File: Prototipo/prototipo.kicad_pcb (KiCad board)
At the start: 2 copper layers, 271.5 x 102.5 mm, 139 parts, among them J1 Conn_01x02_Socket, J4 Conn_01x12_Pin, Q1 MMBT2222A, Q10 MMBT2222A, Q11 MMBT2907A, Q12 MMBT2222A, Q13 MMBT2222A, Q14 MMBT2907A, Q15 MMBT2222A, Q16 MMBT2222A, Q17 MMBT2907A, Q18 MMBT2222A, Q2 MMBT2222A, Q20 FDMS6681Z, Q21 FDMS6681Z, Q3 MMBT2907A, Q4 MMBT2222A, Q5 MMBT2907A, Q6 MMBT2222A, Q7 MMBT2907A, Q8 MMBT2222A, Q9 MMBT2222A

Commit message: Agrega los fusibles en los bancos
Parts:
- added F7: Fuse, Huellas:Fuseholder_Cylinder-5x20mm_Schurter_0031_8201_Horizontal_Open, F.Cu at (675.5, 355.9)
- added F8: Fuse, Huellas:Fuseholder_Cylinder-5x20mm_Schurter_0031_8201_Horizontal_Open, F.Cu at (675.5, 369.0)
- added F9: Fuse, Huellas:Fuseholder_Cylinder-5x20mm_Schurter_0031_8201_Horizontal_Open, F.Cu at (675.5, 342.7)
- moved TP_tierra1 131.5 mm to (387.8, 254.8)
- moved TP_tierra2 131.5 mm to (397.7, 254.5)
- moved TP_tierra3 131.5 mm to (411.0, 254.5)
- moved TP_tierra4 131.5 mm to (424.0, 254.5)
- moved R17 6.16 mm to (484.0, 235.6)
- moved Q9 6.16 mm to (495.6, 237.7)
- moved D1 6.16 mm to (475.8, 245.6)
- moved F3 6.16 mm to (447.5, 239.1)
- moved Q5 6.16 mm to (492.2, 247.1)
- moved R15 6.16 mm to (491.2, 252.3)
- moved R16 6.16 mm to (507.6, 249.3)
- moved R18 6.16 mm to (476.4, 240.1)
- moved ROUT3 6.16 mm to (503.5, 243.1)
- moved TP5 6.16 mm to (468.1, 247.1)
- moved VCELL2 6.16 mm to (515.0, 252.6)
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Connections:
- Q20 pad 5: /celda_1/bus_pos -> Net-(Q20-D_1)
- Q20 pad 6: /celda_1/bus_pos -> Net-(Q20-D_1)
- Q20 pad 7: /celda_1/bus_pos -> Net-(Q20-D_1)
- Q20 pad 8: /celda_1/bus_pos -> Net-(Q20-D_1)
- Q20 pad 9: /celda_1/bus_pos -> Net-(Q20-D_1)
- Q21 pad 5: /celda_3/bus_pos -> Net-(Q21-D_1)
- Q21 pad 6: /celda_3/bus_pos -> Net-(Q21-D_1)
- Q21 pad 7: /celda_3/bus_pos -> Net-(Q21-D_1)
- Q21 pad 8: /celda_3/bus_pos -> Net-(Q21-D_1)
- Q21 pad 9: /celda_3/bus_pos -> Net-(Q21-D_1)
- SB_1 pad 5: /celda_1/bus_neg -> Net-(SB_1-D_1)
- SB_1 pad 6: /celda_1/bus_neg -> Net-(SB_1-D_1)
- SB_1 pad 7: /celda_1/bus_neg -> Net-(SB_1-D_1)
- SB_1 pad 8: /celda_1/bus_neg -> Net-(SB_1-D_1)
- SB_1 pad 9: /celda_1/bus_neg -> Net-(SB_1-D_1)
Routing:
- net /celda_1/bus_pos: track 247.4 -> 366.6 mm
- net /celda_5/bus_pos: track 182.3 -> 191.2 mm
- net /celda_3/bus_pos: track 327.5 -> 333.7 mm
- net /celda_1/bus_neg: track 97.5 -> 101.3 mm
- net /celda_2/cell_neg: track 33.7 -> 37.1 mm
- net /celda_6/cell_neg: track 23.8 -> 26.3 mm
- net Net-(D_B3-+): track 40.4 -> 41.8 mm
- net Net-(QB_5-C): track 16.0 -> 14.6 mm
- net Net-(Q14-B): track 12.9 -> 14.1 mm
- net Net-(QB_1-C): track 16.0 -> 15.0 mm
- net Net-(D_B1-+): track 40.4 -> 41.4 mm
- net Net-(QB_3-C): track 16.0 -> 15.0 mm
- net Net-(D_B2-+): track 40.4 -> 41.4 mm
- net Net-(Q7-B): track 12.9 -> 13.8 mm
- net Net-(Q3-B): track 12.9 -> 13.7 mm
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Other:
- board outline removed

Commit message: termino de reacomodar las celdas con la disposición nueva, faltan las conexiones de la entrada.
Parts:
- removed VCELL3: 3.3, Huellas:BatteryHolder_MPD_BK-18650-PC2
- added TPgnd11: TestPoint, TestPoint:TestPoint_Bridge_Pitch2.54mm_Drill1.0mm, F.Cu at (406.5, 481.8)
- added TPgnd12: TestPoint, TestPoint:TestPoint_Bridge_Pitch2.54mm_Drill1.0mm, F.Cu at (411.5, 391.5)
- added TPgnd21: TestPoint, TestPoint:TestPoint_Bridge_Pitch2.54mm_Drill1.0mm, F.Cu at (460.4, 481.8)
- added TPgnd22: TestPoint, TestPoint:TestPoint_Bridge_Pitch2.54mm_Drill1.0mm, F.Cu at (465.3, 391.2)
- added TPgnd31: TestPoint, TestPoint:TestPoint_Bridge_Pitch2.54mm_Drill1.0mm, F.Cu at (514.2, 481.8)
- added TPgnd32: TestPoint, TestPoint:TestPoint_Bridge_Pitch2.54mm_Drill1.0mm, F.Cu at (518.8, 392.0)
- added VCELL21: 3.3, Huellas:BatteryHolder_MPD_BK-18650-PC2, F.Cu at (490.9, 409.2)
- VCELL11: renamed from VCELL1; moved to F.Cu
- VCELL12: renamed from VCELL2; moved to F.Cu
- VCELL22: renamed from VCELL4; moved to F.Cu
- VCELL31: renamed from VCELL5; moved to F.Cu
- VCELL32: renamed from VCELL6; moved to F.Cu
- moved F1 265.5 mm to (420.0, 428.0), turned to 90 degrees
- moved S31 231.5 mm to (519.8, 452.3)
- moved Q31_1 223.6 mm to (519.5, 482.5), turned to 0 degrees
- moved R31_1 221.2 mm to (525.5, 477.4), turned to -90 degrees
- moved S3 214.7 mm to (510.9, 431.5), turned to 180 degrees
- moved S21 214.2 mm to (465.9, 452.3)
- moved TPC31 213.4 mm to (513.0, 439.5), turned to -90 degrees
- moved D31 212.1 mm to (505.5, 465.8), turned to 90 degrees
- moved Q21_1 211.5 mm to (465.6, 482.5), turned to 0 degrees
- moved F2 210.1 mm to (473.9, 428.1), turned to 90 degrees
- moved R21_1 209.0 mm to (471.6, 477.4), turned to -90 degrees
- moved TPC21 206.7 mm to (459.1, 439.5), turned to -90 degrees
- moved D3 206.7 mm to (509.9, 415.7)
- moved R3_9 206.2 mm to (507.7, 438.8), turned to -90 degrees
- moved TPG31 204.7 mm to (530.2, 469.0), turned to -90 degrees
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- renumbered D_B1 to D1, D4 to D11, D1 to D12, D_B2 to D2, D2 to D21, D3 to D22, D_B3 to D3, D5 to D31, D6 to D32, F7 to F1, F1 to F11, F3 to F12, F8 to F2, F2 to F21, F4 to F22, F9 to F3, F5 to F31, F6 to F32, J4 to IN1, J1 to OUT1, Q1 to Q11_1, Q3 to Q11_2, Q4 to Q11_3, Q2 to Q12_1, Q5 to Q12_2, Q9 to Q12_3, QB_1 to Q1_1, QB_2 to Q1_2, Q6 to Q21_1, Q7 to Q21_2, Q8 to Q21_3, Q10 to Q22_1, Q11 to Q22_2, Q12 to Q22_3, QB_3 to Q2_1, QB_4 to Q2_2, Q13 to Q31_1, Q14 to Q31_2, Q15 to Q31_3, Q16 to Q32_1, Q17 to Q32_2, Q18 to Q32_3, QB_5 to Q3_1, QB_6 to Q3_2, R7 to R11_1, R8 to R11_2, R9 to R11_3, R1 to R11_4, R12 to R11_5, R10 to R11_6, R13 to R12_1, R14 to R12_2, R15 to R12_3, R17 to R12_4, R18 to R12_5, R16 to R12_6, RB_2 to R1_7, RB_3 to R1_8, RB_1 to R1_9, R2 to R21_1, R3 to R21_2, R4 to R21_3, R6 to R21_4, R11 to R21_5, R5 to R21_6, R19 to R22_1, R20 to R22_2, R21 to R22_3, R23 to R22_4, R24 to R22_5, R22 to R22_6, RB_5 to R2_7, RB_6 to R2_8, RB_4 to R2_9, R25 to R31_1, R26 to R31_2, R27 to R31_3, R29 to R31_4, R30 to R31_5, R28 to R31_6, R31 to R32_1, R32 to R32_2, R33 to R32_3, R35 to R32_4, R36 to R32_5, R34 to R32_6, RB_8 to R3_7, RB_9 to R3_8, RB_7 to R3_9, ROUT1 to Rout11, ROUT3 to Rout12, ROUT2 to Rout21, ROUT4 to Rout22, ROUT5 to Rout31, ROUT6 to Rout32, SB_1 to S1, S4 to S11, S1 to S12, Q20 to S2, S2 to S21, S3 to S22, Q21 to S3, S5 to S31, S6 to S32, SGND11 to Sgnd11, SGND1 to Sgnd21, TP9 to TPB11, TP11 to TPB12, TP10 to TPB21, TP12 to TPB22, TP13 to TPB31, TP14 to TPB32, TP18 to TPC11, TP20 to TPC12, TP19 to TPC21, TP21 to TPC22, TP22 to TPC31, TP23 to TPC32, TP15 to TPG1, TP3 to TPG11, TP5 to TPG12, TP16 to TPG2, TP4 to TPG21, TP6 to TPG22, TP17 to TPG3, TP7 to TPG31, TP8 to TPG32, TP1 to TPbanco1, TP2 to TPbanco2
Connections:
- net /celda_1/Vcontrol_neg renamed /celda_11/Vcontrol_neg
- net /celda_1/bus_neg renamed /celda_11/bus_neg
- net /celda_1/bus_pos renamed /celda_11/bus_pos
- net /celda_1/cell_neg renamed /celda_11/cell_neg
- net /celda_1/gate renamed /celda_11/gate
- net /celda_2/Vcontrol_neg renamed /celda_12/Vcontrol_neg
- net /celda_2/cell_neg renamed /celda_12/cell_neg
- net /celda_2/gate renamed /celda_12/gate
- net /celda_3/Vcontrol_neg renamed /celda_21/Vcontrol_neg
- net /celda_3/bus_pos renamed /celda_21/bus_pos
- net /celda_3/cell_neg renamed /celda_21/cell_neg
- net /celda_3/gate renamed /celda_21/gate
- net /celda_4/Vcontrol_neg renamed /celda_22/Vcontrol_neg
- net /celda_4/cell_neg renamed /celda_22/cell_neg
- net /celda_4/gate renamed /celda_22/gate
- net /celda_5/Vcontrol_neg renamed /celda_31/Vcontrol_neg
- net /celda_5/bus_pos renamed /celda_31/bus_pos
- net /celda_5/cell_neg renamed /celda_31/cell_neg
- net /celda_5/gate renamed /celda_31/gate
- net /celda_6/Vcontrol_neg renamed /celda_32/Vcontrol_neg
- net /celda_6/cell_neg renamed /celda_32/cell_neg
- net /celda_6/gate renamed /celda_32/gate
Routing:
- net /celda_21/bus_pos: track 333.7 -> 147.8 mm, vias 4 -> 0
- net Net-(J_B1-Pin_2): track 95.7 -> 0.00 mm
- net /celda_31/bus_pos: track 191.2 -> 112.8 mm, vias 4 -> 0
- net /celda_11/bus_pos: track 366.6 -> 295.9 mm, vias 4 -> 0
- net Net-(VCELL21-+): track 11.2 -> 78.3 mm, vias 0 -> 1
- net Net-(VCELL11-+): track 11.2 -> 78.3 mm, vias 0 -> 1
- net Net-(VCELL31-+): track 11.2 -> 78.3 mm, vias 0 -> 1
- net Net-(Q12_1-C): track 3.51 -> 61.4 mm, vias 0 -> 1
- net Net-(Q32_1-C): track 3.51 -> 61.4 mm, vias 0 -> 1
- net Net-(Q22_1-C): track 3.51 -> 61.4 mm, vias 0 -> 1
- net /celda_12/gate: track 100.5 -> 45.9 mm
- net /celda_21/cell_neg: track 32.3 -> 77.9 mm
- net /celda_31/cell_neg: track 32.6 -> 77.9 mm
- net Net-(VCELL22-+): track 11.2 -> 54.9 mm
- net Net-(VCELL32-+): track 11.2 -> 54.9 mm
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
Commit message: Propuesta de conexión de las entradas
no me gusta la opción, pero esta conectado
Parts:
- moved OUT1 368.6 mm to (382.8, 151.2)
- moved J_B2 334.6 mm to (478.2, 152.1)
- moved TPbanco2 241.1 mm to (441.9, 149.3), turned to 0 degrees
- moved J_B1 238.3 mm to (440.1, 153.1), turned to -90 degrees
- moved TP_tierra3 229.2 mm to (365.6, 144.8)
- moved IN1 227.7 mm to (355.8, 188.9), turned to 90 degrees
- moved TP_tierra1 219.2 mm to (474.0, 229.2)
- moved A1 202.0 mm to (364.5, 203.6), turned to 0 degrees
- moved TP_tierra4 199.2 mm to (392.4, 178.2), turned to 90 degrees
- moved R11_1 188.2 mm to (358.1, 298.9), turned to 180 degrees
- moved R22_6 184.8 mm to (451.3, 153.2)
- moved R12_6 184.3 mm to (409.8, 152.7)
- moved TPgnd11 182.5 mm to (371.1, 302.8)
- moved Q1_1 181.0 mm to (376.7, 236.5)
- moved Q2_1 179.7 mm to (430.6, 237.8)
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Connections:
- IN1 pad 6: Vc_12 -> Vc_32
- IN1 pad 8: Vc_32 -> Vc_12
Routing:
- net /celda_31/Vcontrol_neg: track 0.00 -> 237.9 mm
- net Vc_31: track 0.00 -> 218.7 mm, vias 0 -> 1
- net /celda_21/bus_pos: track 147.8 -> 356.4 mm, vias 0 -> 3
- net /celda_21/Vcontrol_neg: track 0.00 -> 190.0 mm
- net Vc_32: track 0.00 -> 178.6 mm, vias 0 -> 1
- net /celda_32/Vcontrol_neg: track 0.00 -> 172.4 mm, vias 0 -> 4
- net Vc_21: track 0.00 -> 170.1 mm, vias 0 -> 1
- net /celda_22/Vcontrol_neg: track 0.00 -> 153.4 mm, vias 0 -> 1
- net /celda_11/Vcontrol_neg: track 0.00 -> 141.4 mm
- net Vc3: track 0.00 -> 139.6 mm, vias 0 -> 1
- net Vc_22: track 0.00 -> 125.1 mm, vias 0 -> 1
- net Vc_11: track 0.00 -> 118.1 mm
- net /celda_12/Vcontrol_neg: track 0.00 -> 109.0 mm, vias 0 -> 1
- net Net-(J_B1-Pin_2): track 0.00 -> 106.4 mm
- net /celda_31/bus_pos: track 112.8 -> 216.9 mm, vias 0 -> 1
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- added copper zone on F.Cu, net 0
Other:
- board outline added: 179.9 x 178.8 mm

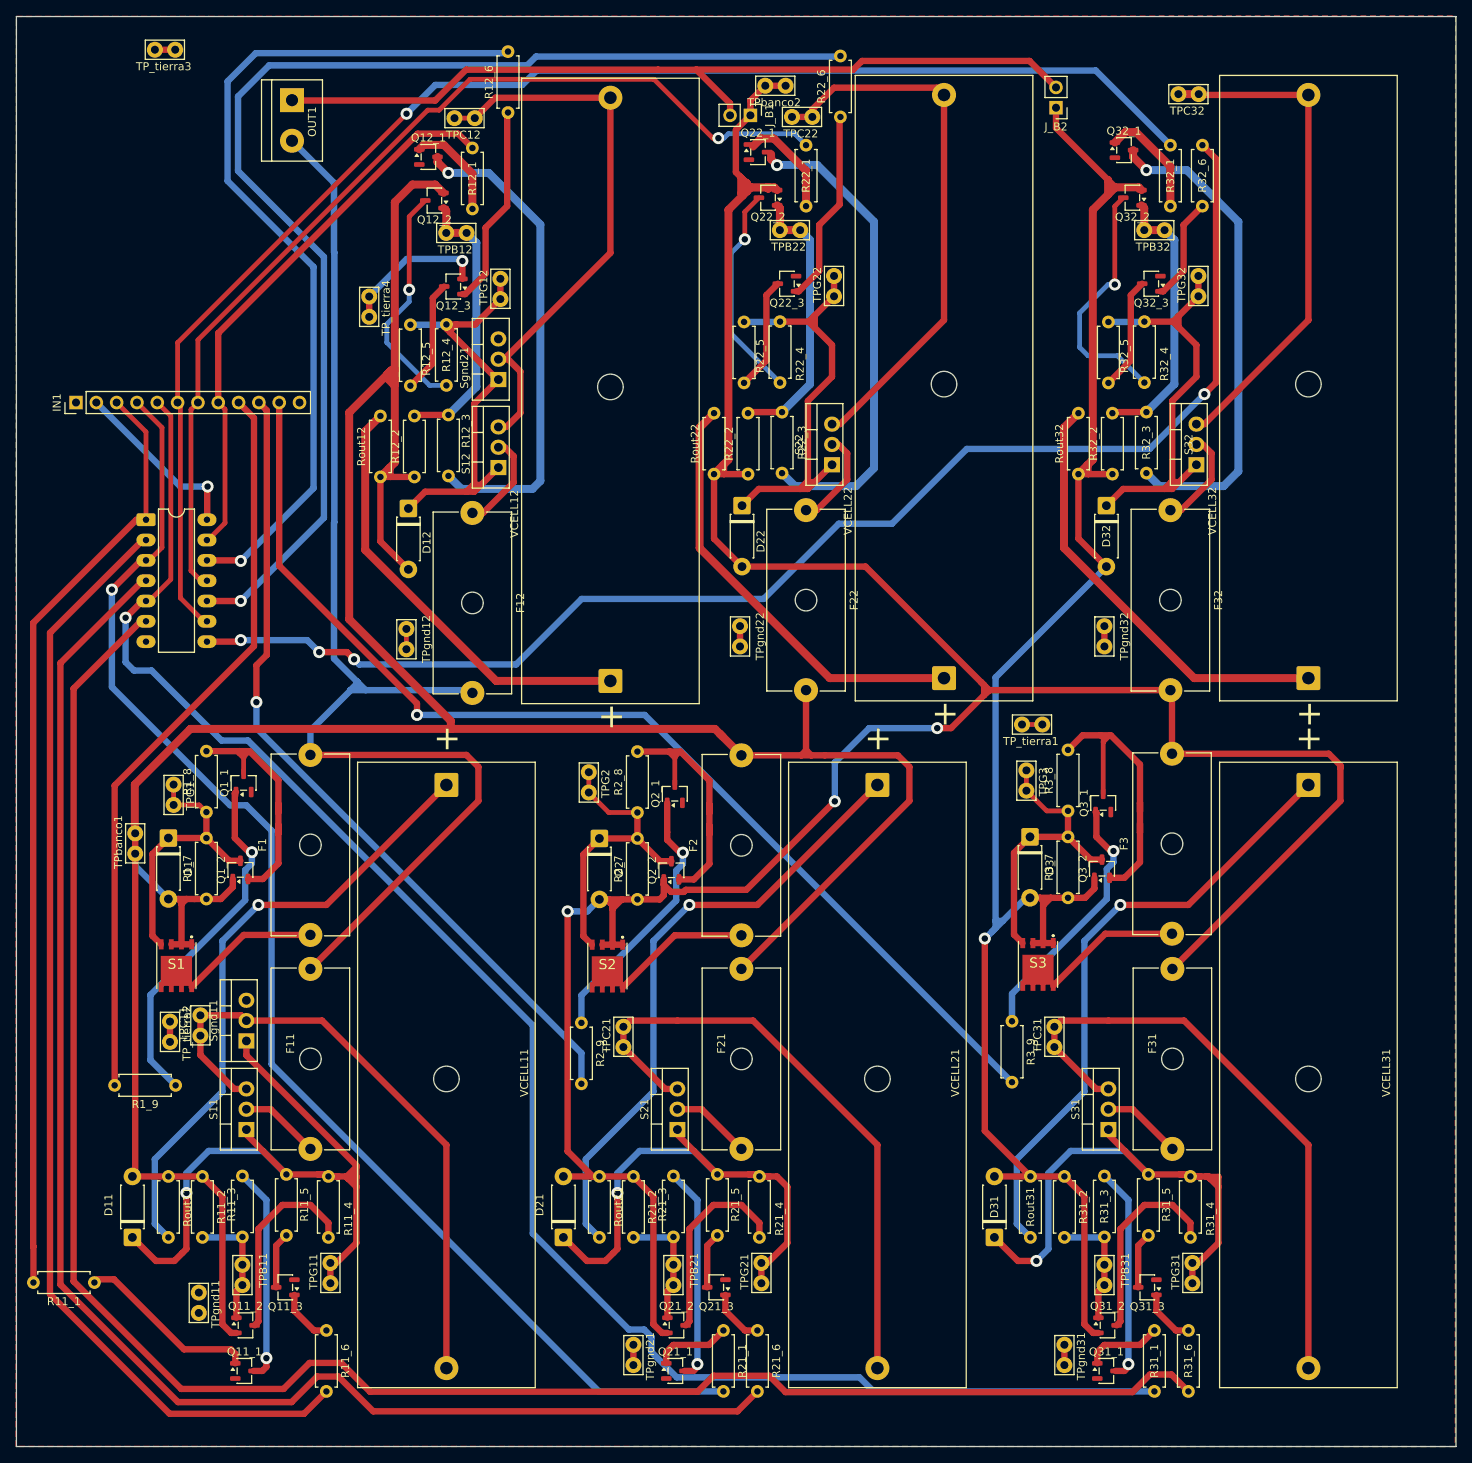
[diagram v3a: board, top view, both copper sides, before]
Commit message: conexión interna de celdas inferiores
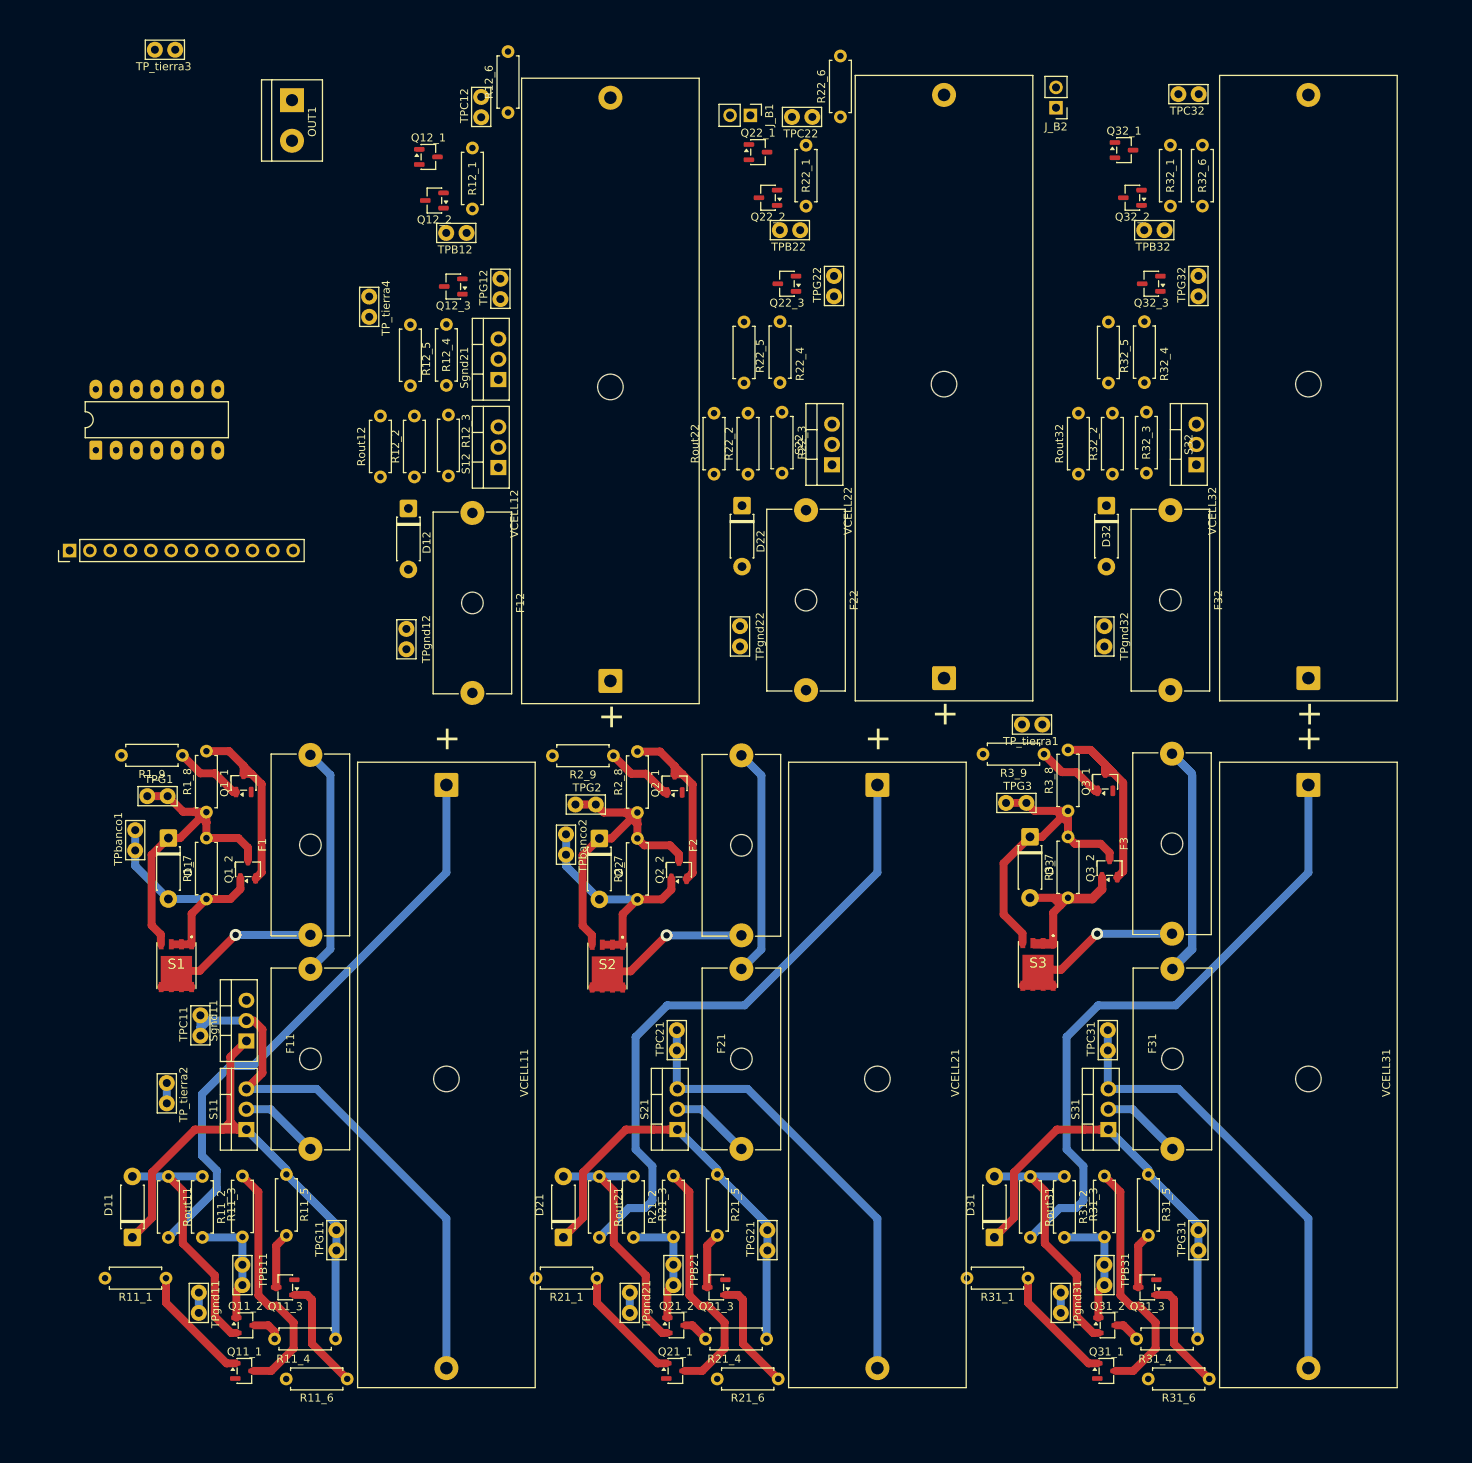
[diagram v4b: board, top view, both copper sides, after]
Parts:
- moved TPbanco2 99.3 mm to (417.0, 245.5), turned to 90 degrees
- moved R1_9 41.3 mm to (369.1, 233.1)
- moved R3_9 33.6 mm to (476.8, 232.9), turned to 180 degrees
- moved R2_9 33.6 mm to (422.9, 233.1), turned to 180 degrees
- moved IN1 18.5 mm to (354.9, 207.4)
- moved R21_1 17.1 mm to (420.9, 298.4), turned to 180 degrees
- moved R31_1 17.1 mm to (474.8, 298.4), turned to 180 degrees
- moved R11_4 14.4 mm to (380.6, 306.0), turned to 0 degrees
- moved R21_4 14.4 mm to (434.5, 306.0), turned to 0 degrees
- moved R31_4 14.4 mm to (488.3, 306.0), turned to 0 degrees
- moved A1 10.7 mm to (358.2, 194.9), turned to 90 degrees
- moved R11_1 8.97 mm to (367.0, 298.4)
- moved TP_tierra2 7.69 mm to (367.1, 276.6)
- moved TPC21 6.69 mm to (430.9, 267.4)
- moved TPC31 6.69 mm to (484.7, 267.4)
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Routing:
- net /celda_11/bus_pos: track 369.7 -> 91.0 mm
- net /celda_31/Vcontrol_neg: track 237.9 -> 0.00 mm
- net /celda_21/bus_pos: track 356.4 -> 119.4 mm, vias 3 -> 0
- net Vc_31: track 218.7 -> 0.00 mm, vias 1 -> 0
- net /celda_21/Vcontrol_neg: track 190.0 -> 0.00 mm
- net Vc_32: track 178.6 -> 0.00 mm, vias 1 -> 0
- net /celda_32/Vcontrol_neg: track 172.4 -> 0.00 mm, vias 4 -> 0
- net Vc_21: track 170.1 -> 0.00 mm, vias 1 -> 0
- net /celda_31/bus_pos: track 216.9 -> 61.6 mm, vias 1 -> 0
- net /celda_22/Vcontrol_neg: track 153.4 -> 0.00 mm, vias 1 -> 0
- net /celda_11/Vcontrol_neg: track 141.4 -> 0.00 mm
- net Vc3: track 139.6 -> 0.00 mm, vias 1 -> 0
- net /celda_11/bus_neg: track 155.6 -> 28.8 mm
- net Vc_22: track 125.1 -> 0.00 mm, vias 1 -> 0
- net Vc_11: track 118.1 -> 0.00 mm
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- removed copper zone on F.Cu, net 0
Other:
- board outline removed
